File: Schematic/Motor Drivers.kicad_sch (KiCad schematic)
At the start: 16 parts, among them U24 DRV8243SQDGQRQ1 (S-Variant), U25 DRV8243SQDGQRQ1 (S-Variant)

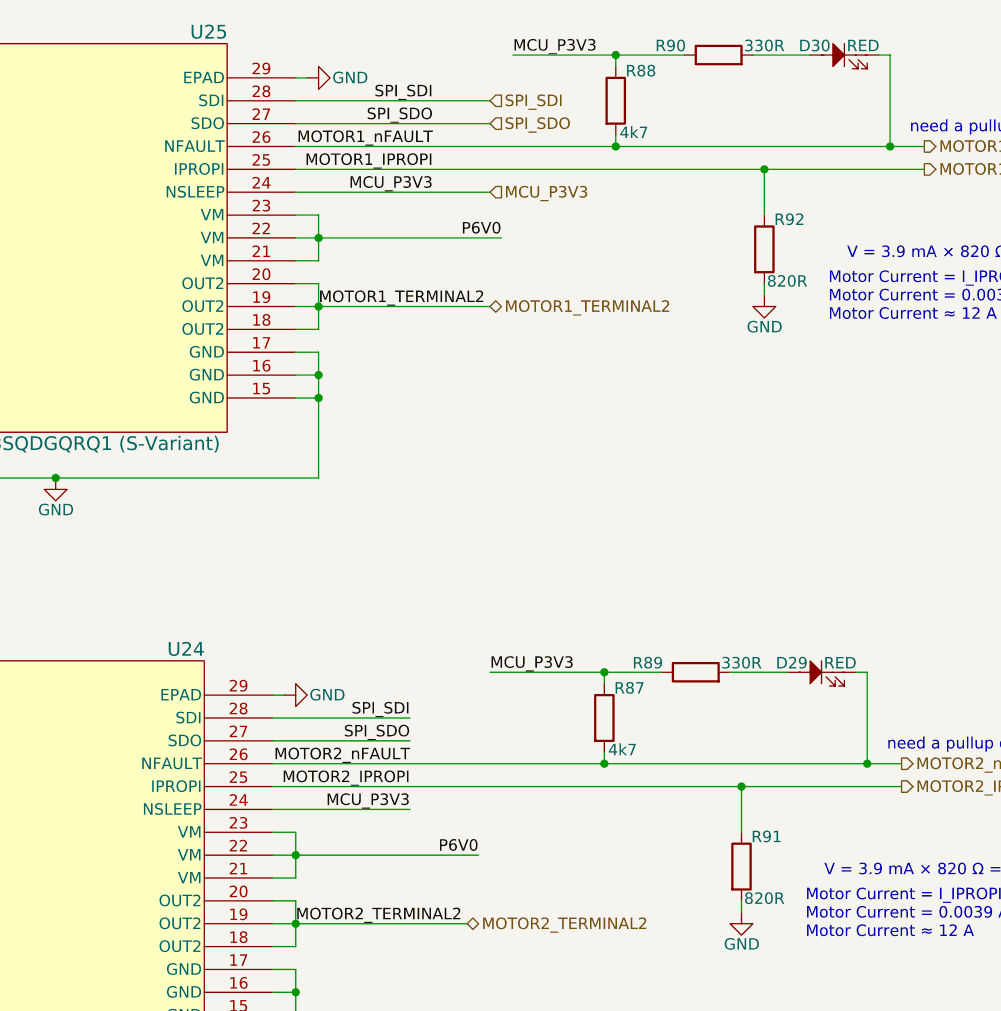
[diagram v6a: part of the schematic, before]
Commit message: added more fets and sense resistor
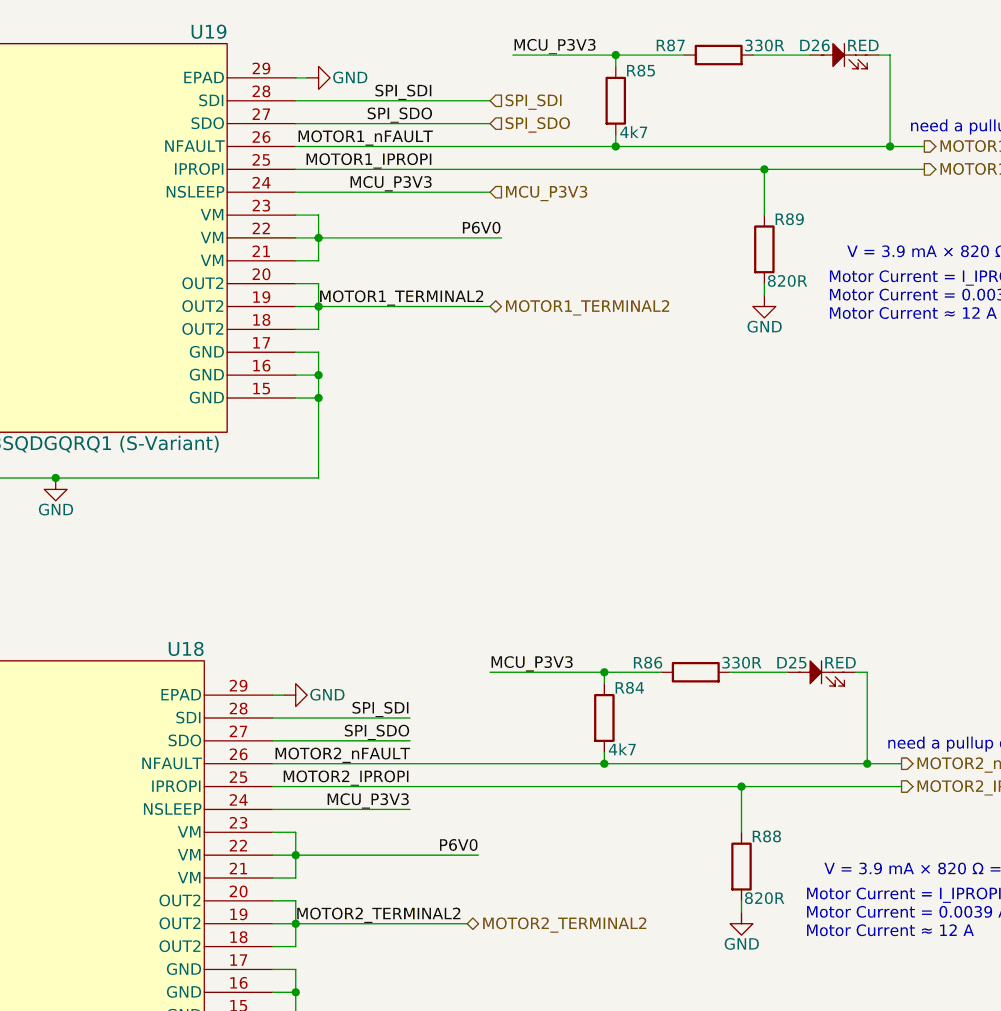
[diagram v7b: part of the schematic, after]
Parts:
- renumbered D29 to D25, D30 to D26, R87 to R84, R88 to R85, R89 to R86, R90 to R87, R91 to R88, R92 to R89, U24 to U18, U25 to U19
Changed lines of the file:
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@@
 		(on_board yes)
 		(dnp no)
-		(property "Reference" "R89"
+		(property "Reference" "R86"
 			(at 208.026 99.314 90)
 			(effects
@@
 			(project "STAR"
 				(path "/fc8533bc-25dd-4c20-9b4c-ffebebd6739b/f73d6367-f3ba-42df-a3ea-bd155f1c219f/07712c52-f5ae-4a00-8c08-8de30640eab9"
-					(reference "R89")
+					(reference "R86")
 					(unit 1)
 				)
@@
 		(on_board yes)
 		(dnp no)
-		(property "Reference" "#PWR065"
+		(property "Reference" "#PWR066"
 			(at 110.49 44.45 0)
 			(effects
@@
 			(project "STAR"
 				(path "/fc8533bc-25dd-4c20-9b4c-ffebebd6739b/f73d6367-f3ba-42df-a3ea-bd155f1c219f/07712c52-f5ae-4a00-8c08-8de30640eab9"
-					(reference "#PWR065")
+					(reference "#PWR066")
 					(unit 1)
 				)
@@
 		(on_board yes)
 		(dnp no)
-		(property "Reference" "#PWR068"
+		(property "Reference" "#PWR069"
 			(at 173.99 102.87 0)
 			(effects
@@
 			(project "STAR"
 				(path "/fc8533bc-25dd-4c20-9b4c-ffebebd6739b/f73d6367-f3ba-42df-a3ea-bd155f1c219f/07712c52-f5ae-4a00-8c08-8de30640eab9"
-					(reference "#PWR068")
+					(reference "#PWR069")
 					(unit 1)
 				)
@@
 		(on_board yes)
 		(dnp no)
-		(property "Reference" "R90"
+		(property "Reference" "R87"
 			(at 210.566 30.734 90)
 			(effects
@@
 			(project "STAR"
 				(path "/fc8533bc-25dd-4c20-9b4c-ffebebd6739b/f73d6367-f3ba-42df-a3ea-bd155f1c219f/07712c52-f5ae-4a00-8c08-8de30640eab9"
-					(reference "R90")
+					(reference "R87")
 					(unit 1)
 				)
@@
 		(on_board yes)
 		(dnp no)
-		(property "Reference" "#PWR069"
+		(property "Reference" "#PWR070"
 			(at 176.53 34.29 0)
 			(effects
@@
 			(project "STAR"
 				(path "/fc8533bc-25dd-4c20-9b4c-ffebebd6739b/f73d6367-f3ba-42df-a3ea-bd155f1c219f/07712c52-f5ae-4a00-8c08-8de30640eab9"
-					(reference "#PWR069")
+					(reference "#PWR070")
 					(unit 1)
 				)
@@
 		(on_board yes)
 		(dnp no)
-		(property "Reference" "U25"
+		(property "Reference" "U19"
 			(at 159.258 29.21 0)
 			(effects
@@
 			(project "STAR"
 				(path "/fc8533bc-25dd-4c20-9b4c-ffebebd6739b/f73d6367-f3ba-42df-a3ea-bd155f1c219f/07712c52-f5ae-4a00-8c08-8de30640eab9"
-					(reference "U25")
+					(reference "U19")
 					(unit 1)
 				)
@@
 		(on_board yes)
 		(dnp no)
-		(property "Reference" "U24"
+		(property "Reference" "U18"
 			(at 156.718 97.79 0)
 			(effects
@@
 			(project "STAR"
 				(path "/fc8533bc-25dd-4c20-9b4c-ffebebd6739b/f73d6367-f3ba-42df-a3ea-bd155f1c219f/07712c52-f5ae-4a00-8c08-8de30640eab9"
-					(reference "U24")
+					(reference "U18")
 					(unit 1)
 				)
@@
 		(on_board yes)
 		(dnp no)
-		(property "Reference" "R92"
+		(property "Reference" "R89"
 			(at 223.774 50.038 0)
 			(effects
@@
 			(project "STAR"
 				(path "/fc8533bc-25dd-4c20-9b4c-ffebebd6739b/f73d6367-f3ba-42df-a3ea-bd155f1c219f/07712c52-f5ae-4a00-8c08-8de30640eab9"
-					(reference "R92")
+					(reference "R89")
 					(unit 1)
 				)
@@
 		(on_board yes)
 		(dnp no)
-		(property "Reference" "D30"
+		(property "Reference" "D26"
 			(at 224.79 30.734 0)
 			(effects
@@
 			(project "STAR"
 				(path "/fc8533bc-25dd-4c20-9b4c-ffebebd6739b/f73d6367-f3ba-42df-a3ea-bd155f1c219f/07712c52-f5ae-4a00-8c08-8de30640eab9"
-					(reference "D30")
+					(reference "D26")
 					(unit 1)
 				)
@@
 		(on_board yes)
 		(dnp no)
-		(property "Reference" "R87"
+		(property "Reference" "R84"
 			(at 205.994 102.108 0)
 			(effects
@@
 			(project "STAR"
 				(path "/fc8533bc-25dd-4c20-9b4c-ffebebd6739b/f73d6367-f3ba-42df-a3ea-bd155f1c219f/07712c52-f5ae-4a00-8c08-8de30640eab9"
-					(reference "R87")
+					(reference "R84")
 					(unit 1)
 				)
@@
 		(on_board yes)
 		(dnp no)
-		(property "Reference" "#PWR066"
+		(property "Reference" "#PWR067"
 			(at 139.7 153.67 0)
 			(effects
@@
 			(project "STAR"
 				(path "/fc8533bc-25dd-4c20-9b4c-ffebebd6739b/f73d6367-f3ba-42df-a3ea-bd155f1c219f/07712c52-f5ae-4a00-8c08-8de30640eab9"
-					(reference "#PWR066")
+					(reference "#PWR067")
 					(unit 1)
 				)
@@
 		(on_board yes)
 		(dnp no)
-		(property "Reference" "#PWR071"
+		(property "Reference" "#PWR072"
 			(at 220.98 64.77 0)
 			(effects
@@
 			(project "STAR"
 				(path "/fc8533bc-25dd-4c20-9b4c-ffebebd6739b/f73d6367-f3ba-42df-a3ea-bd155f1c219f/07712c52-f5ae-4a00-8c08-8de30640eab9"
-					(reference "#PWR071")
+					(reference "#PWR072")
 					(unit 1)
 				)
@@
 		(on_board yes)
 		(dnp no)
-		(property "Reference" "#PWR064"
+		(property "Reference" "#PWR065"
 			(at 107.95 113.03 0)
 			(effects
@@
 			(project "STAR"
 				(path "/fc8533bc-25dd-4c20-9b4c-ffebebd6739b/f73d6367-f3ba-42df-a3ea-bd155f1c219f/07712c52-f5ae-4a00-8c08-8de30640eab9"
-					(reference "#PWR064")
+					(reference "#PWR065")
 					(unit 1)
 				)
@@
 		(on_board yes)
 		(dnp no)
-		(property "Reference" "D29"
+		(property "Reference" "D25"
 			(at 222.25 99.314 0)
 			(effects
@@
 			(project "STAR"
 				(path "/fc8533bc-25dd-4c20-9b4c-ffebebd6739b/f73d6367-f3ba-42df-a3ea-bd155f1c219f/07712c52-f5ae-4a00-8c08-8de30640eab9"
-					(reference "D29")
+					(reference "D25")
 					(unit 1)
 				)
@@
 		(on_board yes)
 		(dnp no)
-		(property "Reference" "#PWR070"
+		(property "Reference" "#PWR071"
 			(at 218.44 133.35 0)
 			(effects
@@
 			(project "STAR"
 				(path "/fc8533bc-25dd-4c20-9b4c-ffebebd6739b/f73d6367-f3ba-42df-a3ea-bd155f1c219f/07712c52-f5ae-4a00-8c08-8de30640eab9"
-					(reference "#PWR070")
+					(reference "#PWR071")
 					(unit 1)
 				)
@@
 		(on_board yes)
 		(dnp no)
-		(property "Reference" "R91"
+		(property "Reference" "R88"
 			(at 221.234 118.618 0)
 			(effects
@@
 			(project "STAR"
 				(path "/fc8533bc-25dd-4c20-9b4c-ffebebd6739b/f73d6367-f3ba-42df-a3ea-bd155f1c219f/07712c52-f5ae-4a00-8c08-8de30640eab9"
-					(reference "R91")
+					(reference "R88")
 					(unit 1)
 				)
@@
 		(on_board yes)
 		(dnp no)
-		(property "Reference" "R88"
+		(property "Reference" "R85"
 			(at 207.264 33.528 0)
 			(effects
@@
 			(project "STAR"
 				(path "/fc8533bc-25dd-4c20-9b4c-ffebebd6739b/f73d6367-f3ba-42df-a3ea-bd155f1c219f/07712c52-f5ae-4a00-8c08-8de30640eab9"
-					(reference "R88")
+					(reference "R85")
 					(unit 1)
 				)
@@
 		(on_board yes)
 		(dnp no)
-		(property "Reference" "#PWR067"
+		(property "Reference" "#PWR068"
 			(at 142.24 85.09 0)
 			(effects
@@
 			(project "STAR"
 				(path "/fc8533bc-25dd-4c20-9b4c-ffebebd6739b/f73d6367-f3ba-42df-a3ea-bd155f1c219f/07712c52-f5ae-4a00-8c08-8de30640eab9"
-					(reference "#PWR067")
+					(reference "#PWR068")
 					(unit 1)
 				)

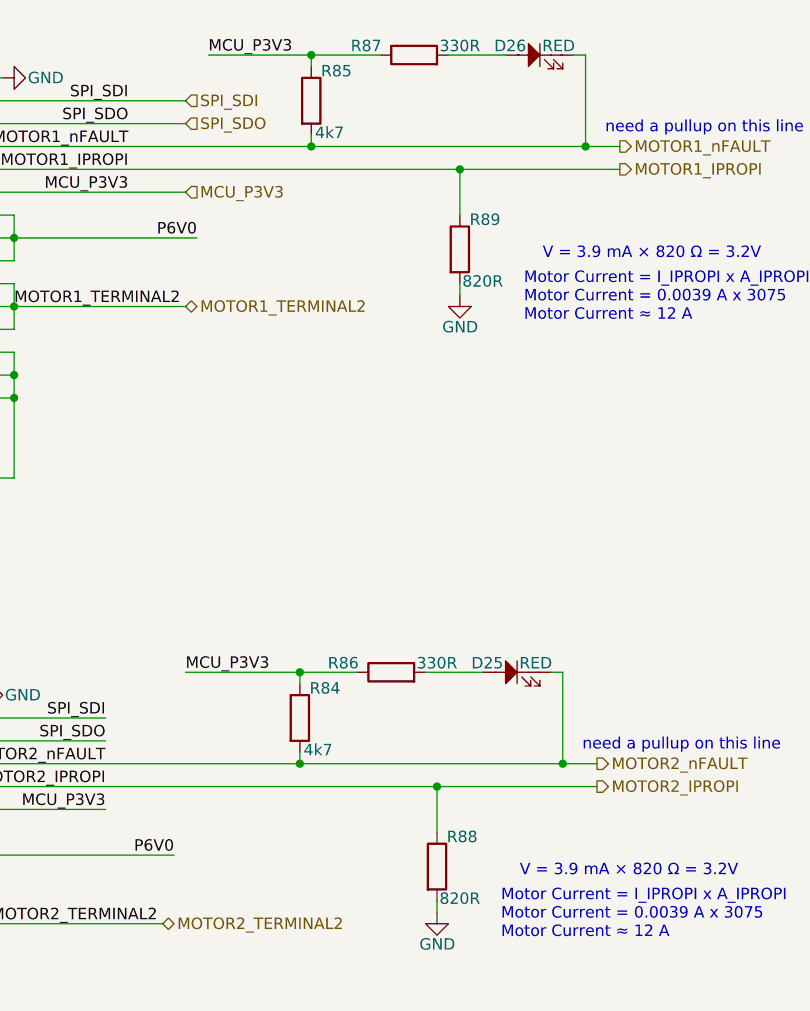
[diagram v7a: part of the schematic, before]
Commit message: added footprints/BOM for resistors and beads
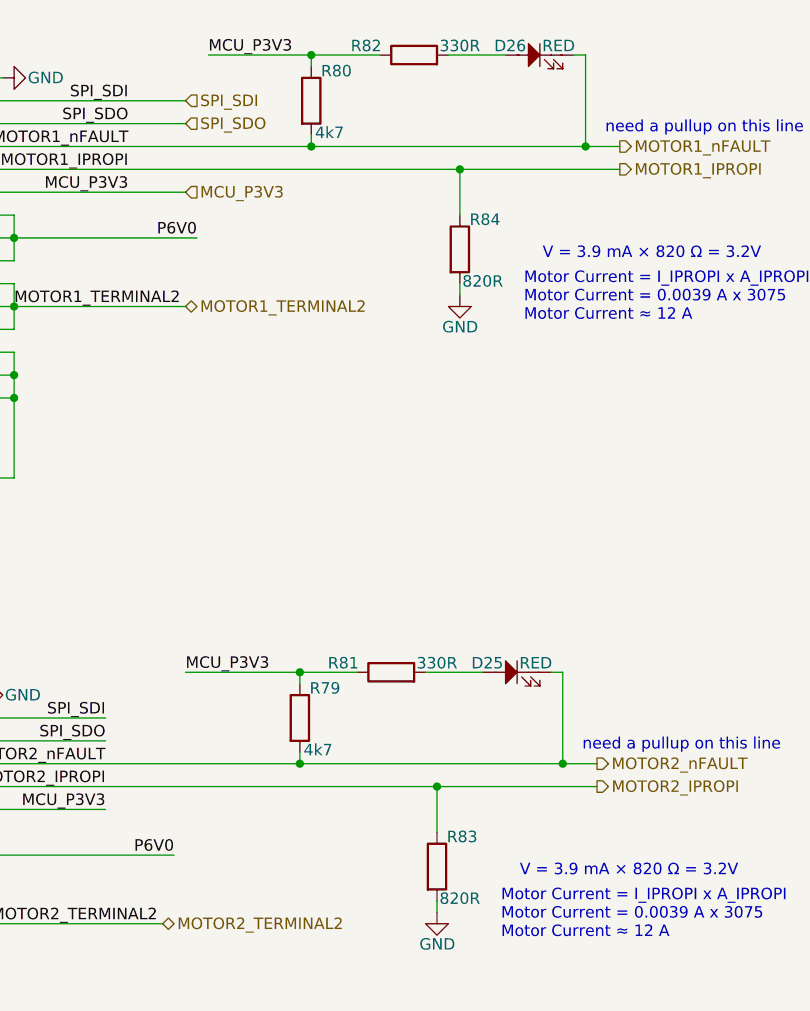
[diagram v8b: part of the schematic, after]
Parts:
- R81: renamed from R86; footprint (none) -> Capacitor_SMD:C_0603_1608Metric_Pad1.08x0.95mm_HandSolder; DigiKey Link (none) -> https://www.digikey.com/short/vqmpz0p3; DigiKey Part Number (none) -> YAG3664CT-ND; DigiKey Price per Unit (none) -> 0.10; Manufactaurer Part Number (none) -> AC0603JR-07330RL; Mouser Link (none) -> https://mou.sr/3VRPQUq; Mouser Part Number (none) -> 603-AC0603JR-07330RL; Mouser Price per Unit (none) -> 0.10
- R83: renamed from R88; Mouser Part Number 791-RMC1/16K8200FTP -> 791-RMC1/16K8200FTP
- R84: renamed from R89; footprint (none) -> Resistor_SMD:R_0603_1608Metric_Pad0.98x0.95mm_HandSolder; DigiKey Link (none) -> N/A; DigiKey Part Number (none) -> N/A; DigiKey Price per Unit (none) -> N/A; Manufactaurer Part Number (none) -> RMC1/16K8200FTP; Mouser Link (none) -> https://mou.sr/46iPyuQ; Mouser Part Number (none) -> 791-RMC1/16K8200FTP; Mouser Price per Unit (none) -> 0.10
- renumbered R84 to R79, R85 to R80, R87 to R82
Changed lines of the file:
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@@
 		(on_board yes)
 		(dnp no)
-		(property "Reference" "R86"
+		(property "Reference" "R81"
 			(at 208.026 99.314 90)
 			(effects
@@
 			)
 		)
-		(property "Footprint" ""
+		(property "Footprint" "Capacitor_SMD:C_0603_1608Metric_Pad1.08x0.95mm_HandSolder"
 			(at 213.36 102.108 90)
 			(effects
@@
 			)
 		)
-		(property "DigiKey Link" ""
+		(property "DigiKey Link" "https://www.digikey.com/short/vqmpz0p3"
 			(at 213.36 100.33 90)
 			(effects
@@
 			)
 		)
-		(property "DigiKey Part Number" ""
+		(property "DigiKey Part Number" "YAG3664CT-ND"
+			(at 213.36 100.33 90)
+			(effects
+				(font
+					(size 1.27 1.27)
+				)
+				(hide yes)
+			)
+		)
+		(property "DigiKey Price per Unit" "0.10"
+			(at 213.36 100.33 90)
+			(effects
+				(font
+					(size 1.27 1.27)
+				)
+				(hide yes)
+			)
+		)
+		(property "Manufactaurer Part Number" "AC0603JR-07330RL"
+			(at 213.36 100.33 90)
+			(effects
+				(font
+					(size 1.27 1.27)
+				)
+				(hide yes)
+			)
+		)
+		(property "Mouser Link" "https://mou.sr/3VRPQUq"
+			(at 213.36 100.33 90)
+			(effects
+				(font
+					(size 1.27 1.27)
+				)
+				(hide yes)
+			)
+		)
+		(property "Mouser Part Number" "603-AC0603JR-07330RL"
+			(at 213.36 100.33 90)
+			(effects
+				(font
+					(size 1.27 1.27)
+				)
+				(hide yes)
+			)
+		)
+		(property "Mouser Price per Unit" "0.10"
 			(at 213.36 100.33 90)
 			(effects
@@
 			(project "STAR"
 				(path "/fc8533bc-25dd-4c20-9b4c-ffebebd6739b/f73d6367-f3ba-42df-a3ea-bd155f1c219f/07712c52-f5ae-4a00-8c08-8de30640eab9"
-					(reference "R86")
+					(reference "R81")
 					(unit 1)
 				)
@@
 		(on_board yes)
 		(dnp no)
-		(property "Reference" "R87"
+		(property "Reference" "R82"
 			(at 210.566 30.734 90)
 			(effects
@@
 			(project "STAR"
 				(path "/fc8533bc-25dd-4c20-9b4c-ffebebd6739b/f73d6367-f3ba-42df-a3ea-bd155f1c219f/07712c52-f5ae-4a00-8c08-8de30640eab9"
-					(reference "R87")
+					(reference "R82")
 					(unit 1)
 				)
@@
 		(on_board yes)
 		(dnp no)
-		(property "Reference" "R89"
+		(property "Reference" "R84"
 			(at 223.774 50.038 0)
 			(effects
@@
 			)
 		)
-		(property "Footprint" ""
+		(property "Footprint" "Resistor_SMD:R_0603_1608Metric_Pad0.98x0.95mm_HandSolder"
 			(at 219.202 53.34 90)
 			(effects
@@
 			)
 		)
-		(property "DigiKey Link" ""
+		(property "DigiKey Link" "N/A"
 			(at 220.98 53.34 0)
 			(effects
@@
 			)
 		)
-		(property "DigiKey Part Number" ""
+		(property "DigiKey Part Number" "N/A"
+			(at 220.98 53.34 0)
+			(effects
+				(font
+					(size 1.27 1.27)
+				)
+				(hide yes)
+			)
+		)
+		(property "DigiKey Price per Unit" "N/A"
+			(at 220.98 53.34 0)
+			(effects
+				(font
+					(size 1.27 1.27)
+				)
+				(hide yes)
+			)
+		)
+		(property "Manufactaurer Part Number" "RMC1/16K8200FTP "
+			(at 220.98 53.34 0)
+			(effects
+				(font
+					(size 1.27 1.27)
+				)
+				(hide yes)
+			)
+		)
+		(property "Mouser Link" "https://mou.sr/46iPyuQ"
+			(at 220.98 53.34 0)
+			(effects
+				(font
+					(size 1.27 1.27)
+				)
+				(hide yes)
+			)
+		)
+		(property "Mouser Part Number" "791-RMC1/16K8200FTP"
+			(at 220.98 53.34 0)
+			(effects
+				(font
+					(size 1.27 1.27)
+				)
+				(hide yes)
+			)
+		)
+		(property "Mouser Price per Unit" "0.10"
 			(at 220.98 53.34 0)
 			(effects
@@
 			(project "STAR"
 				(path "/fc8533bc-25dd-4c20-9b4c-ffebebd6739b/f73d6367-f3ba-42df-a3ea-bd155f1c219f/07712c52-f5ae-4a00-8c08-8de30640eab9"
-					(reference "R89")
+					(reference "R84")
 					(unit 1)
 				)
@@
 		(on_board yes)
 		(dnp no)
-		(property "Reference" "R84"
+		(property "Reference" "R79"
 			(at 205.994 102.108 0)
 			(effects
@@
 			(project "STAR"
 				(path "/fc8533bc-25dd-4c20-9b4c-ffebebd6739b/f73d6367-f3ba-42df-a3ea-bd155f1c219f/07712c52-f5ae-4a00-8c08-8de30640eab9"
-					(reference "R84")
+					(reference "R79")
 					(unit 1)
 				)
@@
 		(on_board yes)
 		(dnp no)
-		(property "Reference" "R88"
+		(property "Reference" "R83"
 			(at 221.234 118.618 0)
 			(effects
@@
 			)
 		)
-		(property "Mouser Part Number" "791-RMC1/16K8200FTP "
+		(property "Mouser Part Number" "791-RMC1/16K8200FTP"
 			(at 218.44 121.92 0)
 			(effects
@@
 			(project "STAR"
 				(path "/fc8533bc-25dd-4c20-9b4c-ffebebd6739b/f73d6367-f3ba-42df-a3ea-bd155f1c219f/07712c52-f5ae-4a00-8c08-8de30640eab9"
-					(reference "R88")
+					(reference "R83")
 					(unit 1)
 				)
@@
 		(on_board yes)
 		(dnp no)
-		(property "Reference" "R85"
+		(property "Reference" "R80"
 			(at 207.264 33.528 0)
 			(effects
@@
 			(project "STAR"
 				(path "/fc8533bc-25dd-4c20-9b4c-ffebebd6739b/f73d6367-f3ba-42df-a3ea-bd155f1c219f/07712c52-f5ae-4a00-8c08-8de30640eab9"
-					(reference "R85")
+					(reference "R80")
 					(unit 1)
 				)
